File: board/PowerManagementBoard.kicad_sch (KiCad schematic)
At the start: 0 parts

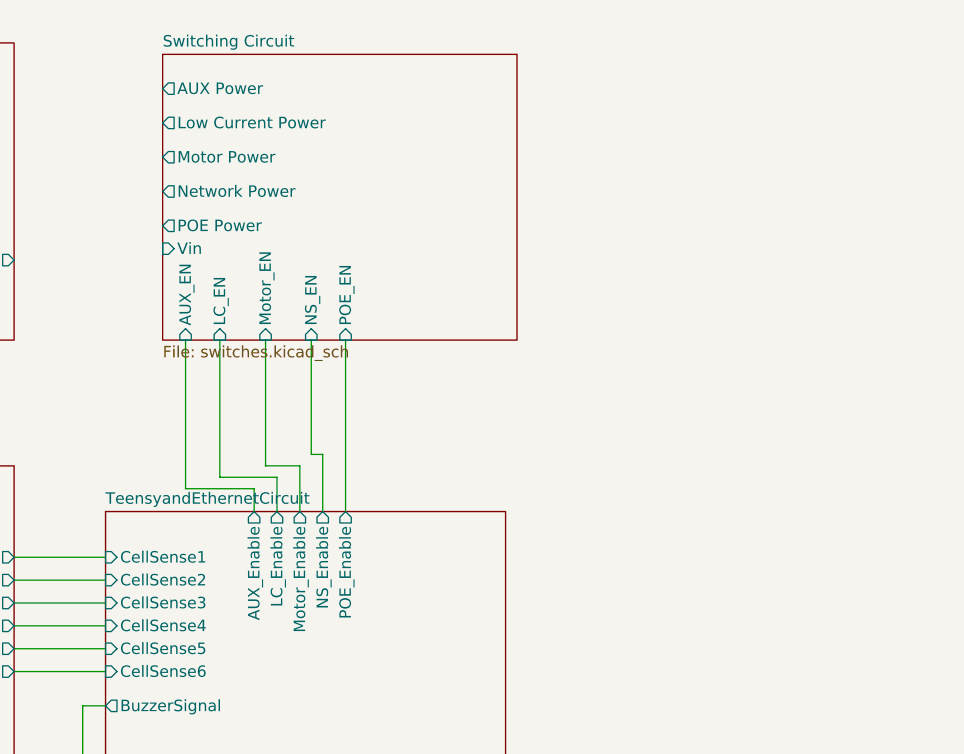
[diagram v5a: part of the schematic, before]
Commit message: Current Sensors FABRICATED
Current Sensor Hierarchy sheet created
Contains:
- Network Switch current sensing
- POE current sensing
- Low Current current sensing
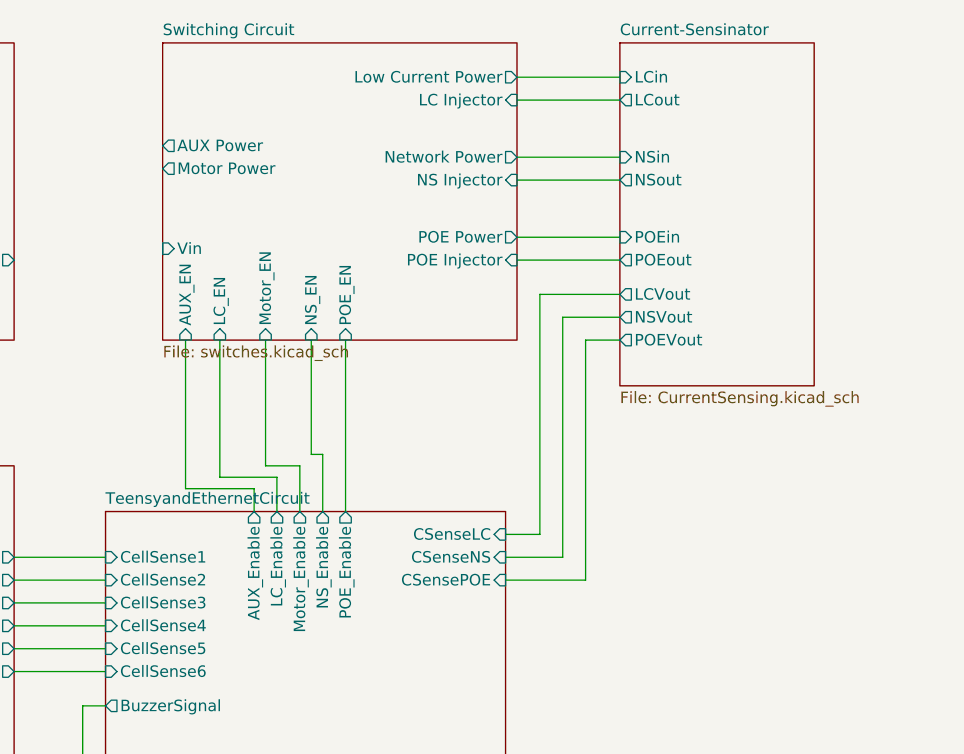
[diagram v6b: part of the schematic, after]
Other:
- added sheet Current-Sensinator (CurrentSensing.kicad_sch)
- sheet Switching Circuit ports: added LC Injector, NS Injector, POE Injector; removed none
- sheet TeensyandEthernetCircuit ports: added CSenseLC, CSenseNS, CSensePOE; removed none

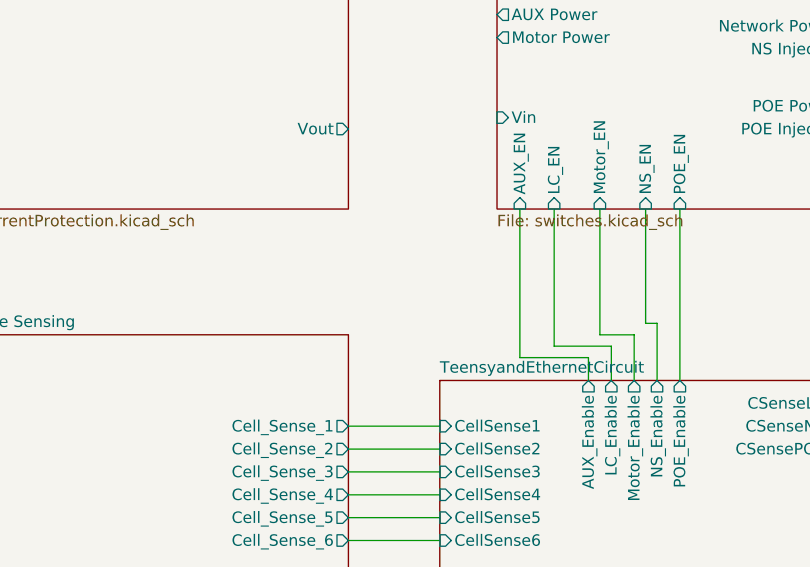
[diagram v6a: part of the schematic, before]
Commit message: BattCSense added
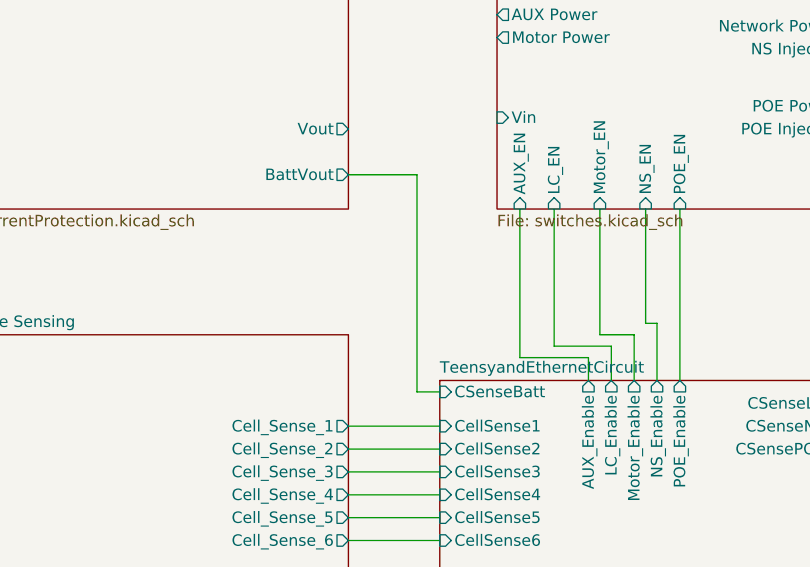
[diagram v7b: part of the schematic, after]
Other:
- sheet Current Protection ports: added BattVout; removed none
- sheet TeensyandEthernetCircuit ports: added CSenseBatt; removed none
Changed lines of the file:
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@@
+	(wire
+		(pts
+			(xy 74.93 78.74) (xy 77.47 78.74)
+		)
+		(stroke
+			(width 0)
+			(type default)
+		)
+	)
 	(wire
 		(pts
@@
 	(wire
 		(pts
+			(xy 74.93 54.61) (xy 74.93 78.74)
+		)
+		(stroke
+			(width 0)
+			(type default)
+		)
+	)
+	(wire
+		(pts
 			(xy 90.17 58.42) (xy 90.17 73.66)
 		)
@@
 		(pts
 			(xy 130.81 85.09) (xy 130.81 58.42)
+		)
+		(stroke
+			(width 0)
+			(type default)
+		)
+	)
+	(wire
+		(pts
+			(xy 67.31 54.61) (xy 74.93 54.61)
 		)
 		(stroke
@@
 			)
 		)
+		(pin "CSenseBatt" input
+			(at 77.47 78.74 180)
+			(effects
+				(font
+					(size 1.27 1.27)
+				)
+				(justify left)
+			)
+		)
 		(instances
 			(project "PowerManagementBoard"
@@
 			(effects
 				(font
+					(size 1.27 1.27)
+				)
+				(justify right)
+			)
+		)
+		(pin "BattVout" output
+			(at 67.31 54.61 0)
+			(effects
+				(font

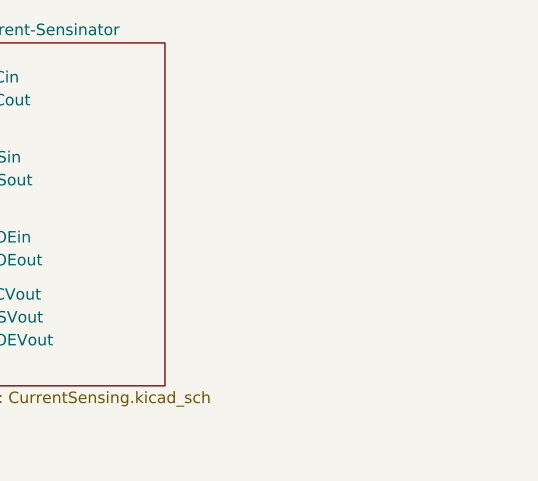
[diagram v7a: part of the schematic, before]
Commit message: add new poe page
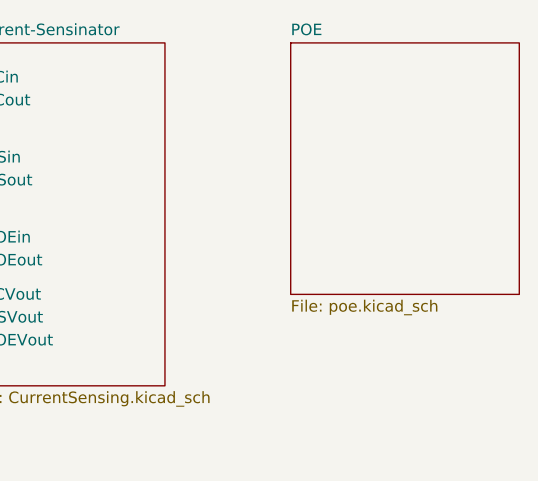
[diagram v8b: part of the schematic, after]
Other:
- added sheet POE (poe.kicad_sch)
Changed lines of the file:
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@@
+	)
+	(sheet
+		(at 170.18 25.4)
+		(size 25.4 27.94)
+		(exclude_from_sim no)
+		(in_bom yes)
+		(on_board yes)
+		(dnp no)
+		(fields_autoplaced yes)
+		(stroke
+			(width 0.1524)
+			(type solid)
+		)
+		(fill
+			(color 0 0 0 0.0000)
+		)
+		(property "Sheetname" "POE"
+			(at 170.18 24.6884 0)
+			(effects
+				(font
+					(size 1.27 1.27)
+				)
+				(justify left bottom)
+			)
+		)
+		(property "Sheetfile" "poe.kicad_sch"
+			(at 170.18 53.9246 0)
+			(effects
+				(font
+					(size 1.27 1.27)
+				)
+				(justify left top)
+			)
+		)
+		(instances
+			(project "PowerManagementBoard"
+				(path "/7eaa639d-7062-45e7-be05-1c2855431307"
+					(page "8")
+				)
+			)
+		)
 	)
 	(sheet
